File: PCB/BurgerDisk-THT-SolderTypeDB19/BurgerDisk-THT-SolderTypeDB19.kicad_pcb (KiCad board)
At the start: 2 copper layers, 93.7 x 67.6 mm, 18 parts, among them J1 Daisy port in, J2 MicroSD module, J3 UART, J4 Daisy port out, U1 PC817

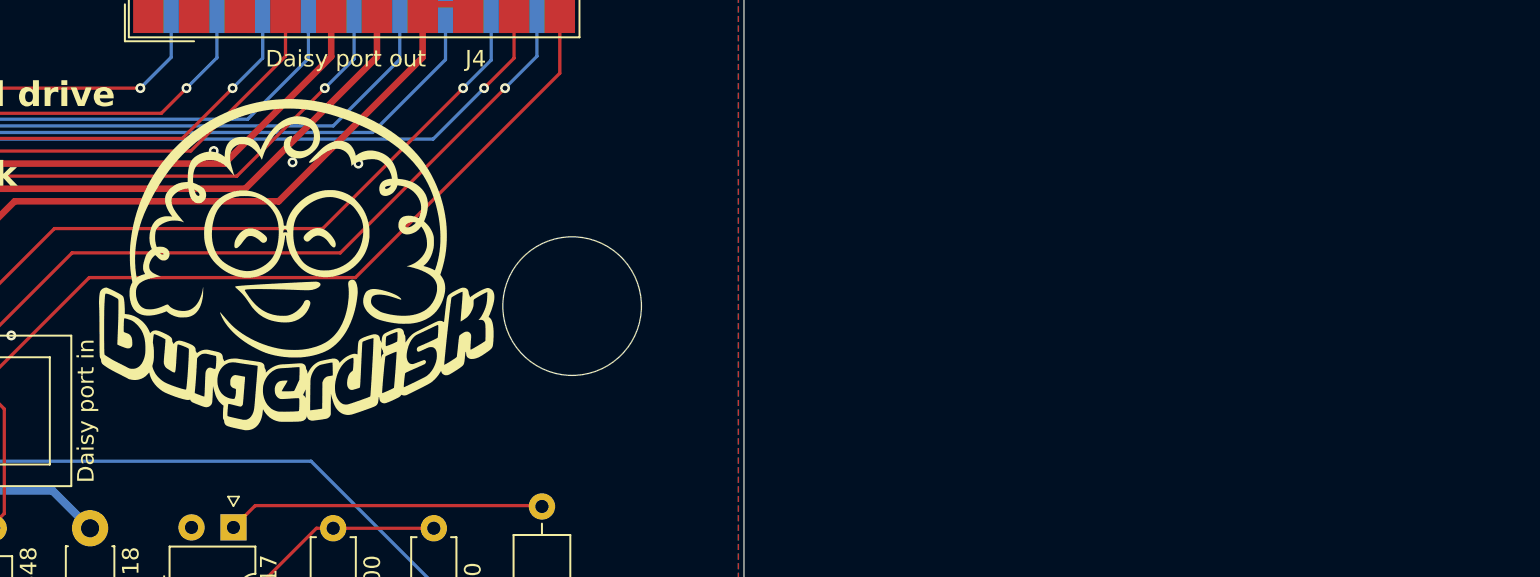
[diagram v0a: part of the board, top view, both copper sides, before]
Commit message: Move logo out of PCB
until I'm sure Rebecca's estate is OK with it
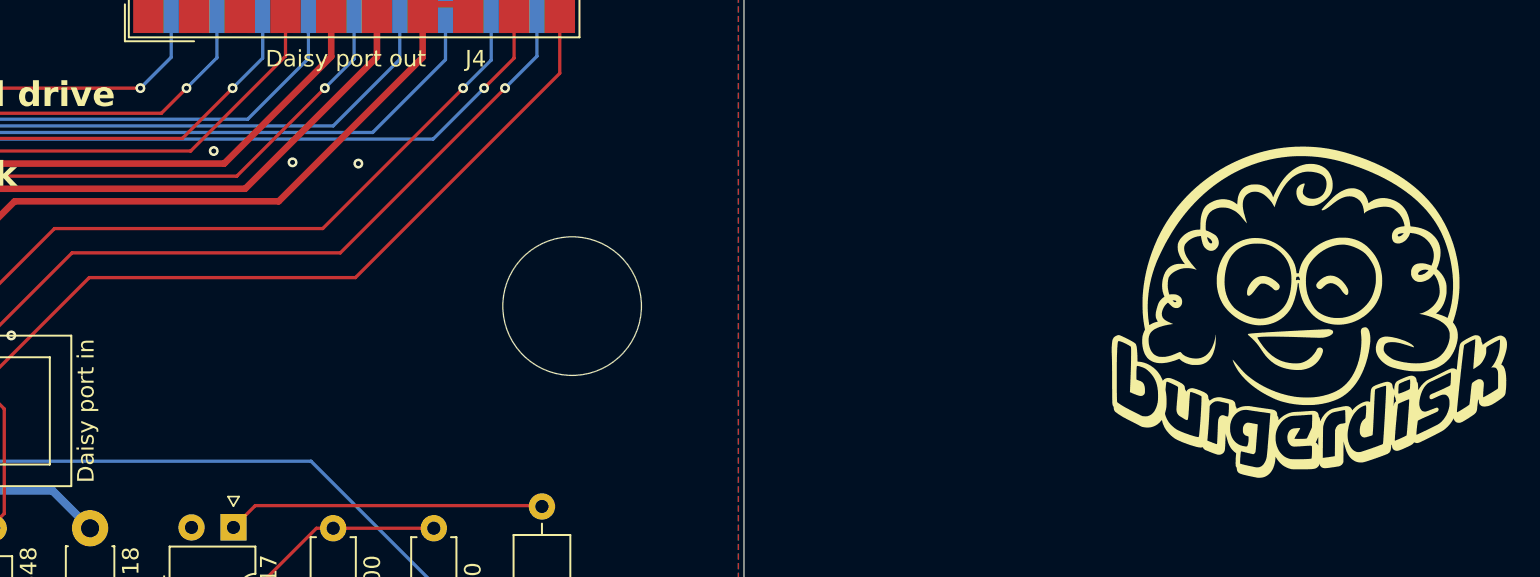
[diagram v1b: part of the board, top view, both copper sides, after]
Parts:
- moved G*** 61.4 mm to (198.8, 64.5)
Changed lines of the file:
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@@
 	(footprint "LOGO"
 		(layer "F.Cu")
-		(at 137.4648 61.5696)
+		(at 198.829486 64.451489)
 		(property "Reference" "G***"
 			(at 0 0 0)

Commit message: OCD
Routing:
- net SCK: track 29.2 -> 20.5 mm
- net 5V_burgerDisk: track 82.3 -> 78.0 mm
- net MOSI: track 21.5 -> 19.5 mm
- net MISO: track 20.1 -> 19.6 mm
- net GND: vias 27 -> 29

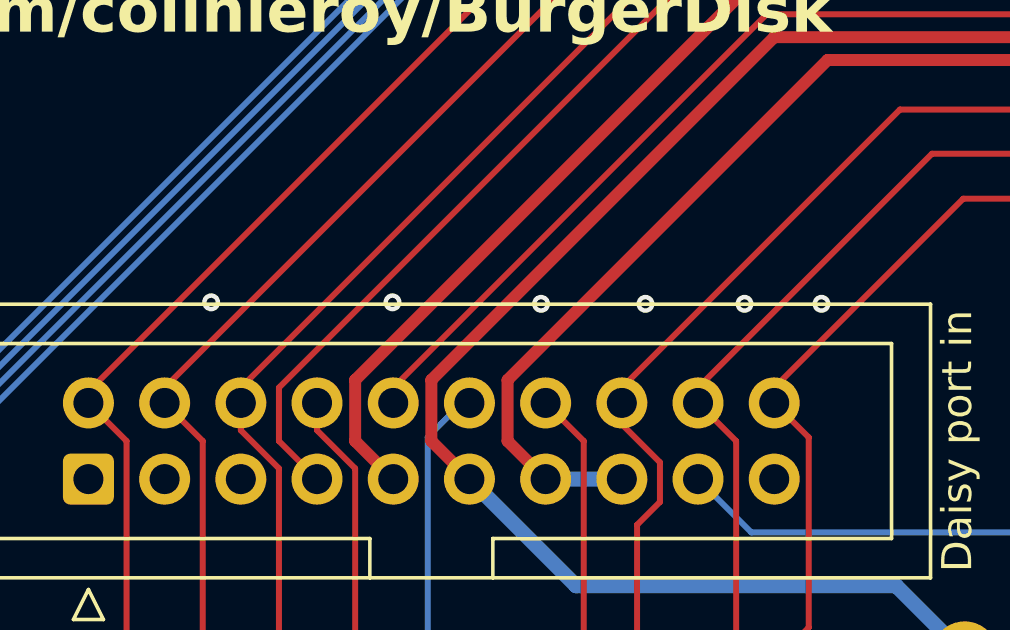
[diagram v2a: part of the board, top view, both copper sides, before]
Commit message: Add via/silkscreen DRC
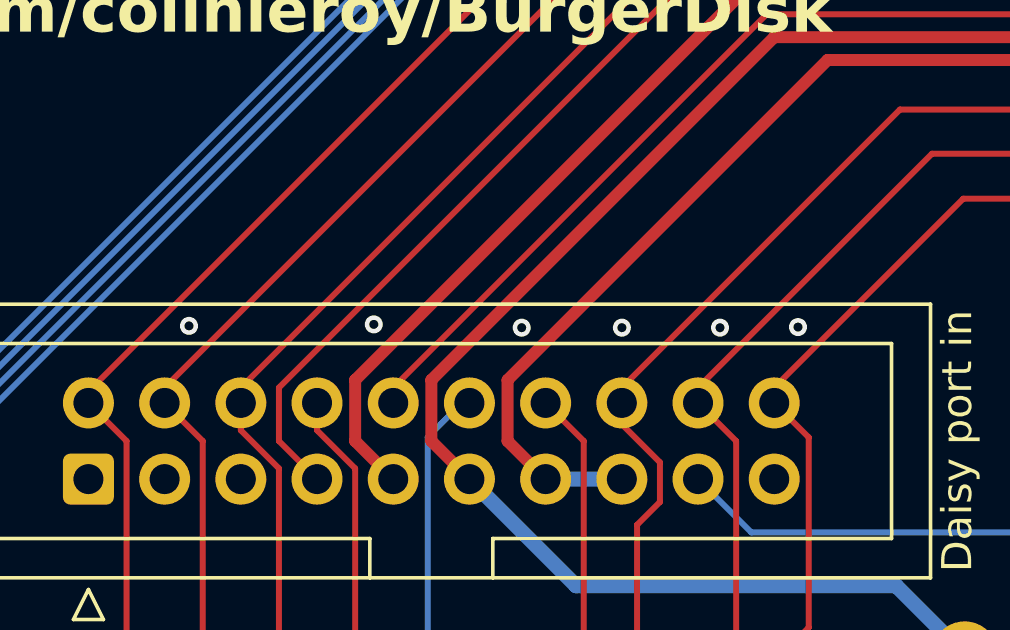
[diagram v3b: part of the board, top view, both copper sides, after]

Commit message: Update details
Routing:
- net DRV1_out: track 124.6 -> 122.2 mm
- net HDSEL_out: track 125.9 -> 123.5 mm
- net 5V_burgerDisk: track 78.0 -> 80.4 mm
- net WREQ: track 47.0 -> 45.7 mm
- net RDDATA_in: track 91.1 -> 89.9 mm
- net DRV2_in: track 44.3 -> 45.5 mm
- net 5V_apple2: track 69.2 -> 68.3 mm
- net HDSEL_in: track 9.87 -> 9.09 mm
- net -12V: track 50.0 -> 49.3 mm
- net Net-(R4-Pad2): track 17.8 -> 18.5 mm
- net WRPROT_in: track 42.8 -> 43.5 mm
- net PH1: track 86.4 -> 85.9 mm
- net WRPROT_out: track 56.5 -> 56.0 mm
- net WRDATA: track 91.2 -> 90.7 mm
- net PH2: track 86.7 -> 86.2 mm
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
